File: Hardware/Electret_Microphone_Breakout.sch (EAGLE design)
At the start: 17 parts, among them M1 MIC9.7MM, U1 OPA344

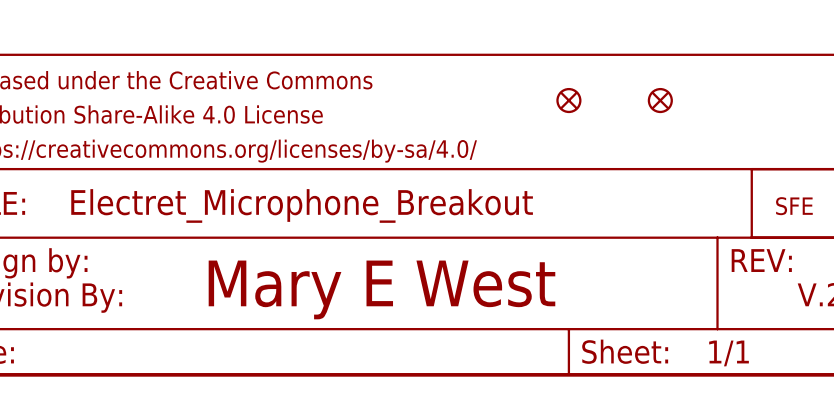
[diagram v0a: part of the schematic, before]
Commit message: Updated Board layout, removed 10 mils of board, went though DRU checklist
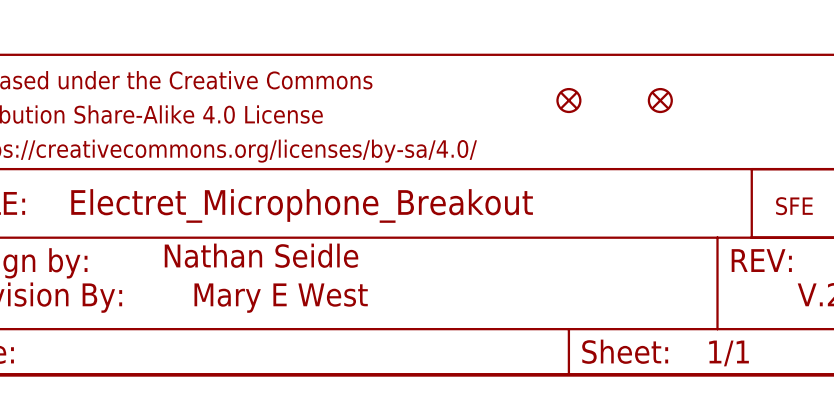
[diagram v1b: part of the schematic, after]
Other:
- note added: "Nathan Seidle"
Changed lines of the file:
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@@
 <text x="152.4" y="139.7" size="1.778" layer="91">VCC 3.3V - 5V</text>
 <text x="243.84" y="7.62" size="2.54" layer="94">V.2</text>
-<text x="177.8" y="7.62" size="5.08" layer="94">Mary E West</text>
+<text x="176.53" y="7.62" size="2.54" layer="94">Mary E West</text>
+<text x="173.228" y="11.938" size="2.54" layer="94">Nathan Seidle</text>
 </plain>
 <instances>

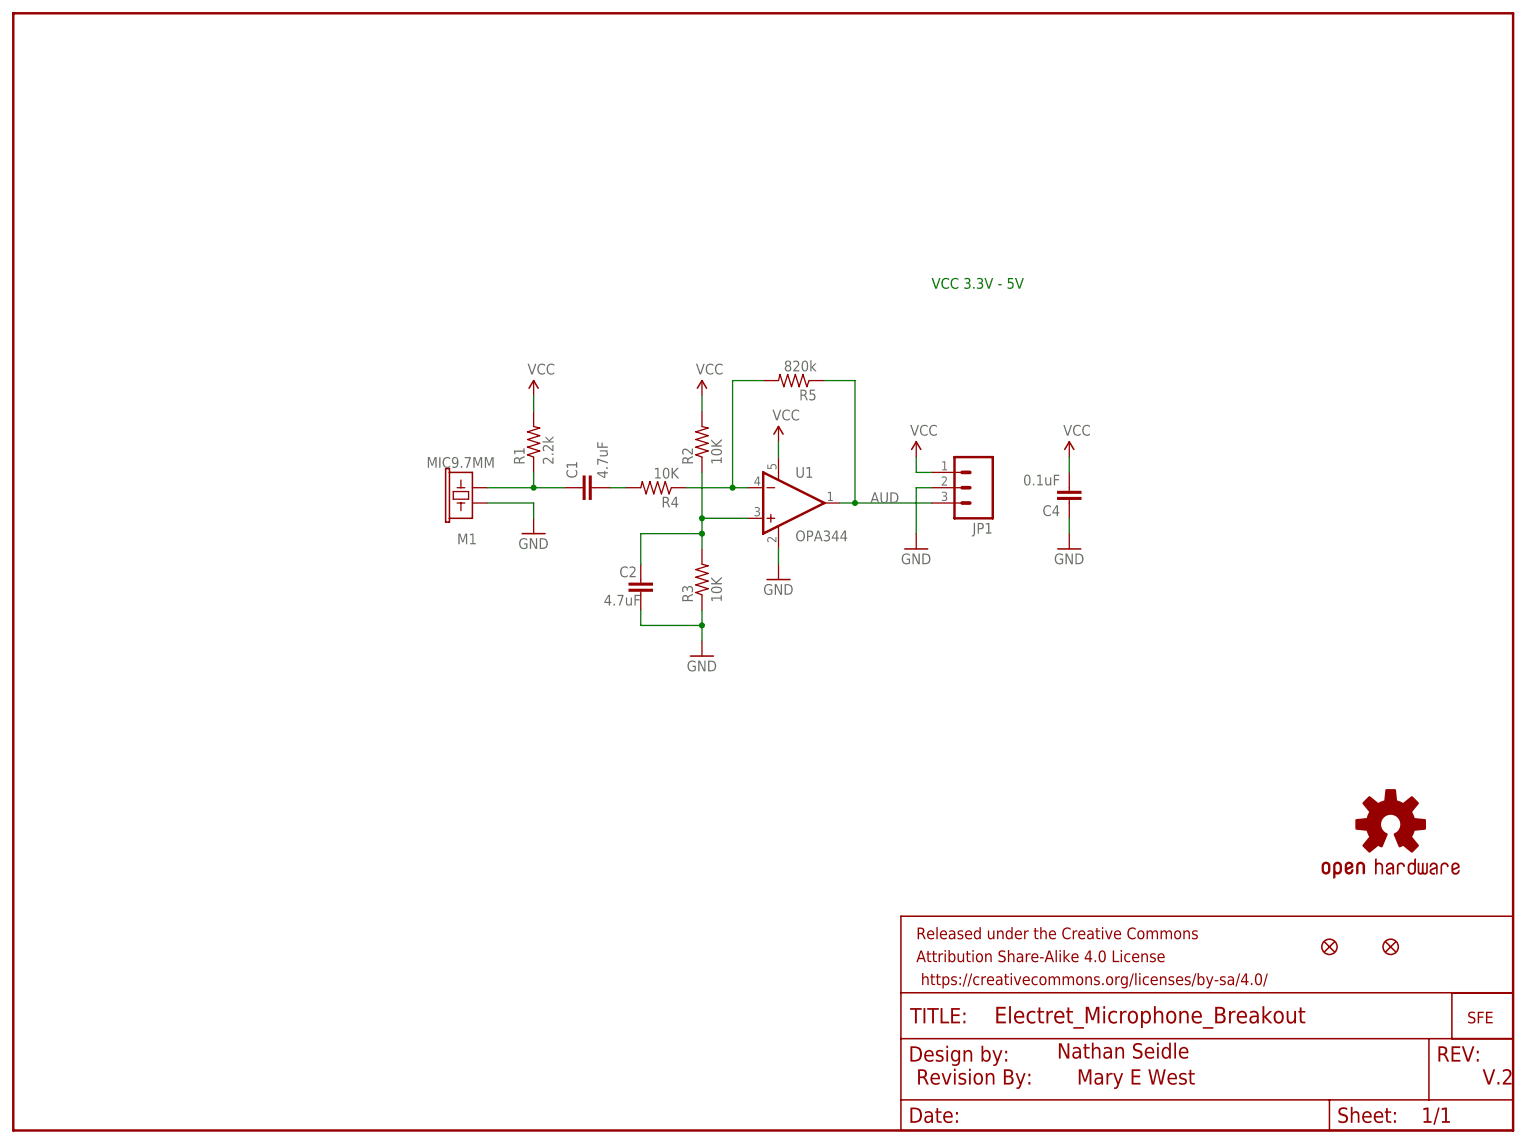
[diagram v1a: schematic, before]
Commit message: Updated Board and Schematic per QC Review 2/12/2016
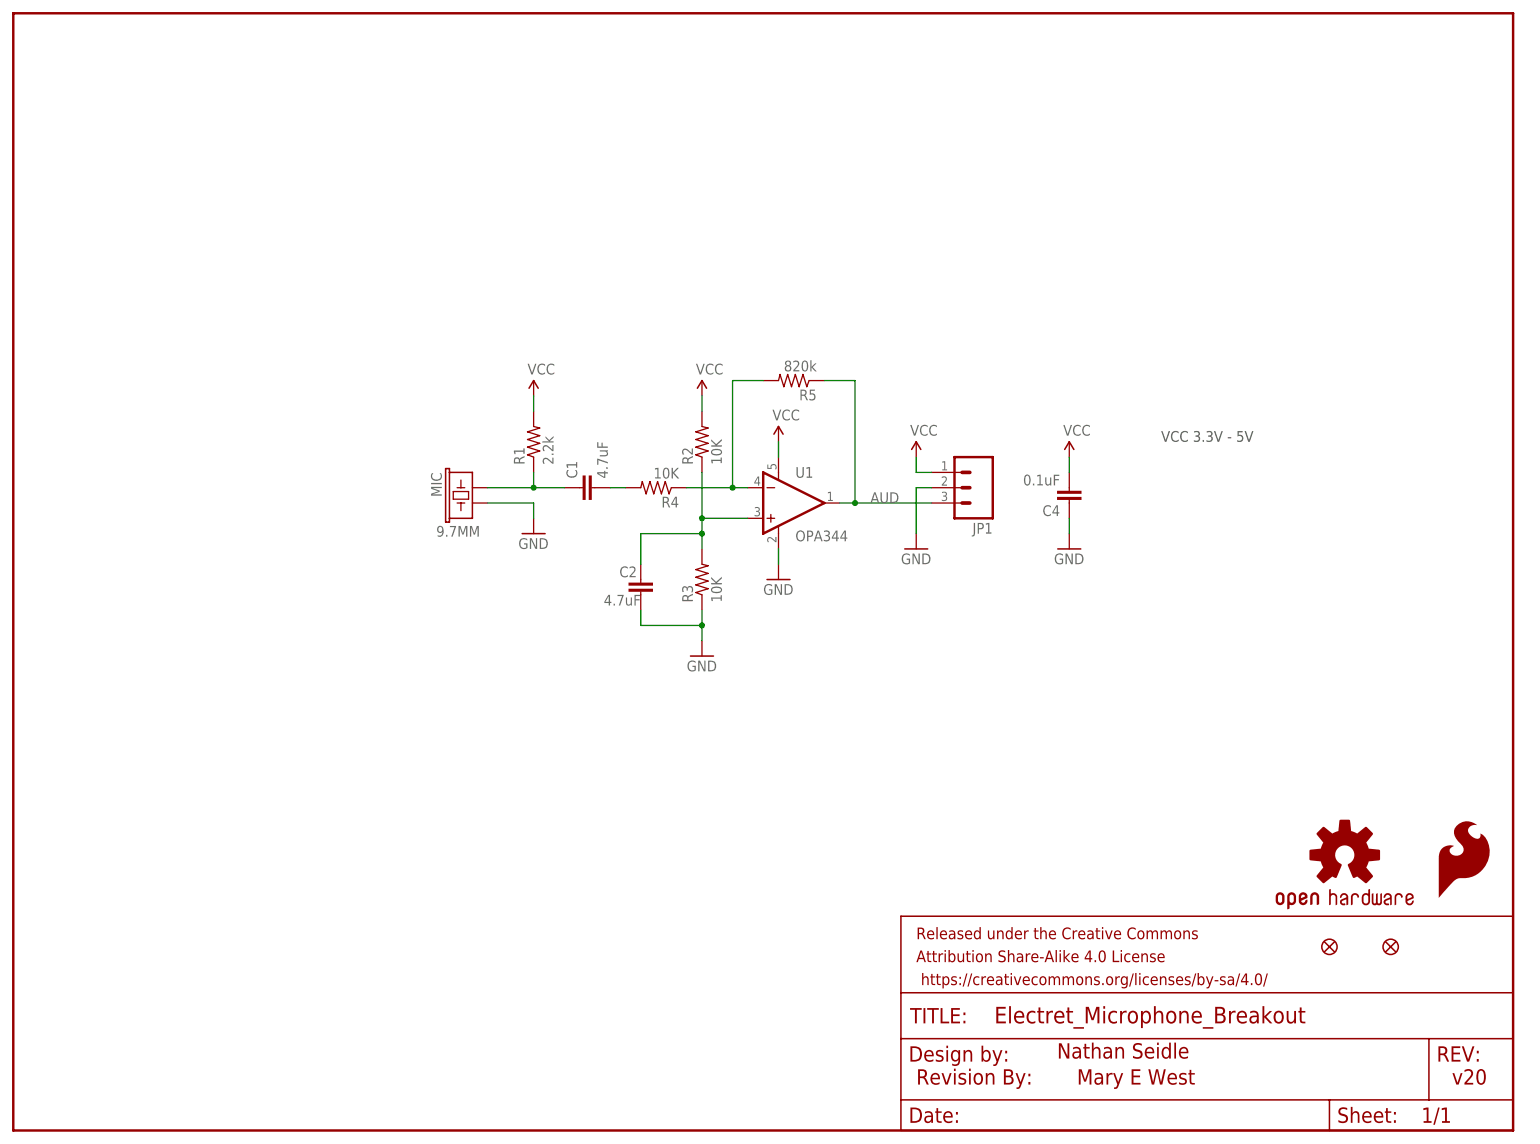
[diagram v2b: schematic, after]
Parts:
- U$1: value LOGO-SFESK -> SFE_LOGO_FLAME.1_INCH; device SparkFun:LOGO-SFESK -> SparkFun-Aesthetics:SFE_LOGO_FLAME.1_INCH
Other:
- note added: "v20"
- note removed: "V.2"
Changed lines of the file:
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@@
 <part name="GND2" library="SparkFun" deviceset="GND" device=""/>
 <part name="P+3" library="SparkFun" deviceset="VCC" device=""/>
-<part name="U$1" library="SparkFun" deviceset="LOGO-SFE" device="SK"/>
+<part name="U$1" library="SparkFun-Aesthetics" deviceset="SFE_LOGO_FLAME" device=".1_INCH" value="SFE_LOGO_FLAME.1_INCH"/>
 <part name="R2" library="SparkFun-Resistors" deviceset="10KOHM-1/10W-1%(0603)" device="0603" value="10K"/>
 <part name="R3" library="SparkFun-Resistors" deviceset="10KOHM-1/10W-1%(0603)" device="0603" value="10K"/>
@@
 <sheet>
 <plain>
-<text x="152.4" y="139.7" size="1.778" layer="91">VCC 3.3V - 5V</text>
-<text x="243.84" y="7.62" size="2.54" layer="94">V.2</text>
+<text x="190.5" y="114.3" size="1.778" layer="97">VCC 3.3V - 5V</text>
+<text x="238.76" y="7.62" size="2.54" layer="94">v20</text>
 <text x="176.53" y="7.62" size="2.54" layer="94">Mary E West</text>
 <text x="173.228" y="11.938" size="2.54" layer="94">Nathan Seidle</text>
@@
 <instance part="FRAME1" gate="G$1" x="0" y="0"/>
 <instance part="FRAME1" gate="V" x="147.32" y="0"/>
-<instance part="M1" gate="G$1" x="76.2" y="106.68" smashed="yes" rot="MR270">
-<attribute name="NAME" x="73.66" y="99.06" size="1.778" layer="95" rot="MR180"/>
-<attribute name="VALUE" x="68.58" y="111.76" size="1.778" layer="96" rot="MR180"/>
-</instance>
+<instance part="M1" gate="MIC" x="76.2" y="106.68" smashed="yes" rot="MR270"/>
 <instance part="U1" gate="G$1" x="127" y="104.14" smashed="yes">
 <attribute name="NAME" x="129.794" y="110.109" size="1.778" layer="95" rot="MR180"/>
@@
 <instance part="GND2" gate="1" x="149.86" y="96.52"/>
 <instance part="P+3" gate="1" x="86.36" y="121.92"/>
-<instance part="U$1" gate="G$1" x="241.3" y="17.78"/>
+<instance part="U$1" gate="G$1" x="236.22" y="38.1"/>
 <instance part="R2" gate="G$1" x="114.3" y="114.3" rot="R90"/>
 <instance part="R3" gate="G$1" x="114.3" y="91.44" rot="R90"/>
@@
 <instance part="JP2" gate="G$1" x="228.6" y="30.48"/>
 <instance part="JP3" gate="G$1" x="218.44" y="30.48"/>
-<instance part="LOGO1" gate="G$1" x="228.6" y="50.8"/>
+<instance part="LOGO1" gate="G$1" x="220.98" y="45.72"/>
 <instance part="U$2" gate="G$1" x="149.86" y="7.62"/>
 </instances>
@@
 <pinref part="C1" gate="G$1" pin="1"/>
 <pinref part="R1" gate="G$1" pin="1"/>
-<pinref part="M1" gate="G$1" pin="1"/>
+<pinref part="M1" gate="MIC" pin="1"/>
 </segment>
 </net>
@@
 <wire x1="86.36" y1="104.14" x2="78.74" y2="104.14" width="0.1524" layer="91"/>
 <pinref part="GND5" gate="1" pin="GND"/>
-<pinref part="M1" gate="G$1" pin="2"/>
+<pinref part="M1" gate="MIC" pin="2"/>
 </segment>
 </net>

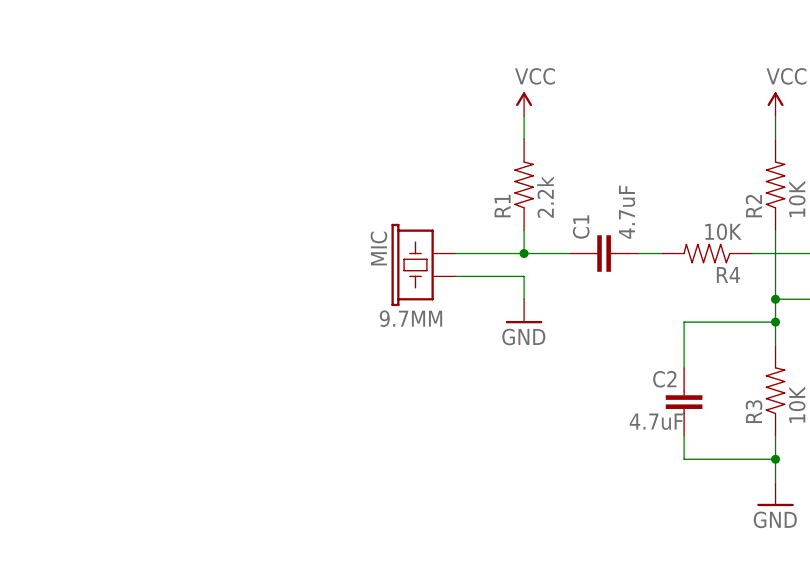
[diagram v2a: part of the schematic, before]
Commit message: Updated Board File - updated MIC Package
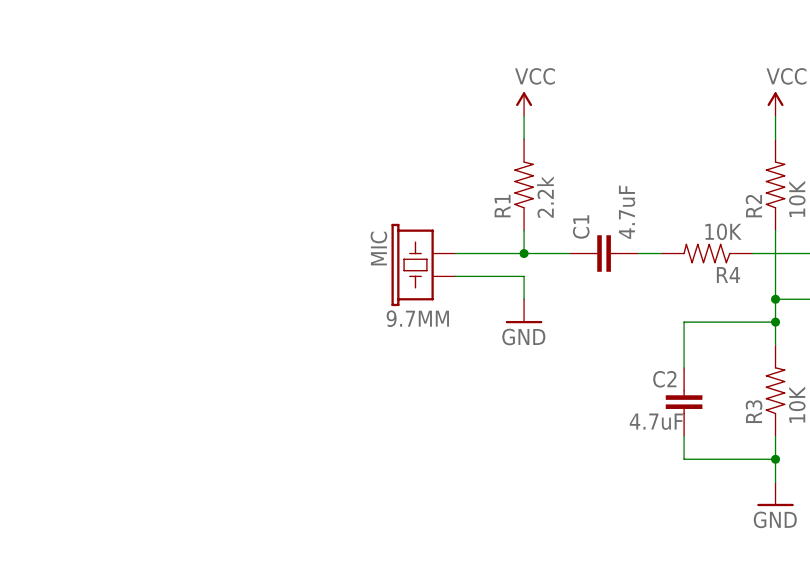
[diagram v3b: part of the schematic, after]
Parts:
- removed M1: MIC9.7MM, SparkFun-Sensors:MIC9.7MM
- added MIC: 9.7MM, SparkFun-Sensors:MIC9.7MM
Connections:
- net GND: now also MIC.2; no longer M1.2
- net N$1: now also MIC.1; no longer M1.1
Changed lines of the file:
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@@
 <parts>
 <part name="FRAME1" library="SparkFun-Aesthetics" deviceset="FRAME-LETTER" device=""/>
-<part name="M1" library="SparkFun-Sensors" deviceset="MIC" device="9.7MM"/>
+<part name="MIC" library="SparkFun-Sensors" deviceset="MIC" device="9.7MM" value="9.7MM"/>
 <part name="U1" library="SparkFun-AnalogIC" deviceset="OPA344" device=""/>
 <part name="C1" library="SparkFun-Capacitors" deviceset="4.7UF-6.3V-10%(0603)" device="0603" value="4.7uF"/>
@@
 <instance part="FRAME1" gate="G$1" x="0" y="0"/>
 <instance part="FRAME1" gate="V" x="147.32" y="0"/>
-<instance part="M1" gate="MIC" x="76.2" y="106.68" smashed="yes" rot="MR270"/>
+<instance part="MIC" gate="&gt;NAME" x="76.2" y="106.68" rot="MR270"/>
 <instance part="U1" gate="G$1" x="127" y="104.14" smashed="yes">
 <attribute name="NAME" x="129.794" y="110.109" size="1.778" layer="95" rot="MR180"/>
@@
 <pinref part="C1" gate="G$1" pin="1"/>
 <pinref part="R1" gate="G$1" pin="1"/>
-<pinref part="M1" gate="MIC" pin="1"/>
+<pinref part="MIC" gate="&gt;NAME" pin="1"/>
 </segment>
 </net>
@@
 <wire x1="86.36" y1="104.14" x2="78.74" y2="104.14" width="0.1524" layer="91"/>
 <pinref part="GND5" gate="1" pin="GND"/>
-<pinref part="M1" gate="MIC" pin="2"/>
+<pinref part="MIC" gate="&gt;NAME" pin="2"/>
 </segment>
 </net>
